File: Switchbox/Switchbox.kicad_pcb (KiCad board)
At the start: 4 copper layers, 90 x 68 mm, 42 parts, among them J1 USB-C_connector, SW1 SW_SPDT, SW2 SW_SPDT, SW3 SW_SPDT, SW4 SW_SPDT, SW5 SW_SPST_LED, SW6 SW_SPDT_BOX, U2 AP63203WU

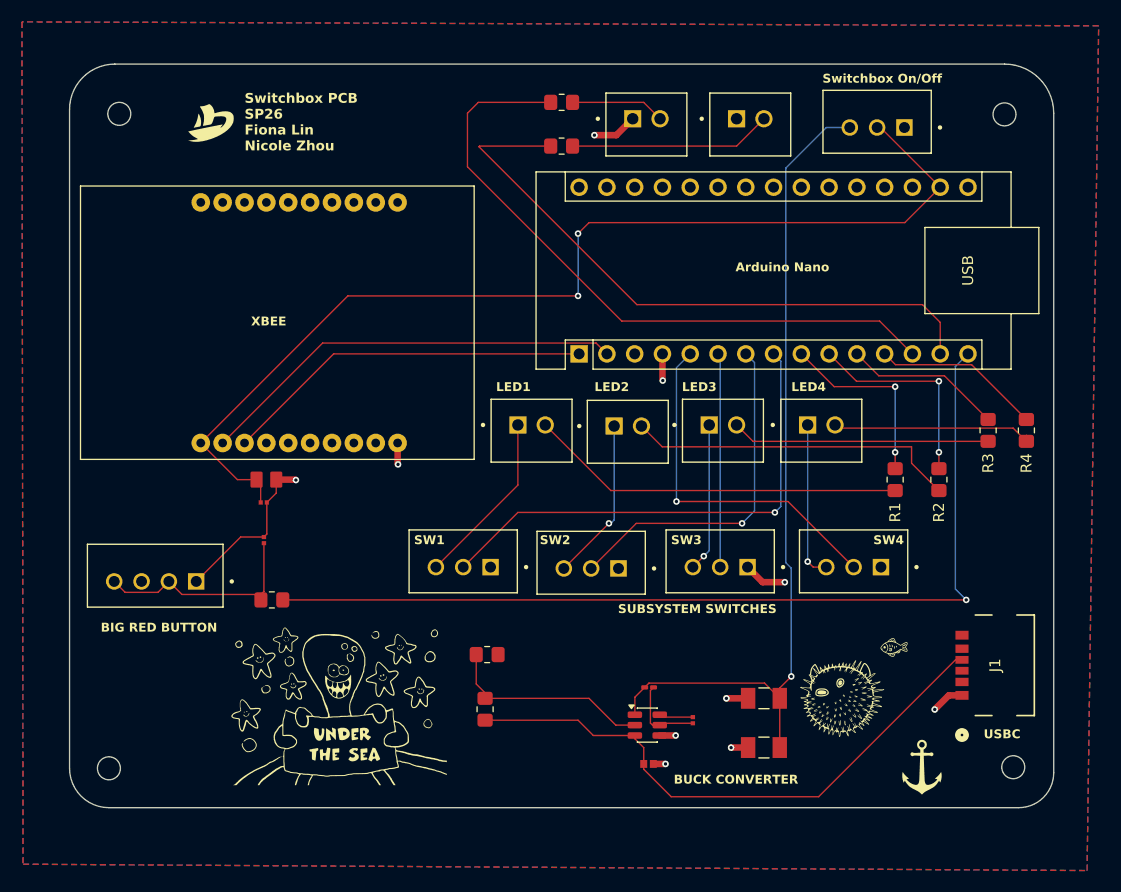
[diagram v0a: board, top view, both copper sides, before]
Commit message: Change USB signals, inductor footprint, add voltage divider between Xbee and Nano, route new components, increase trace widths
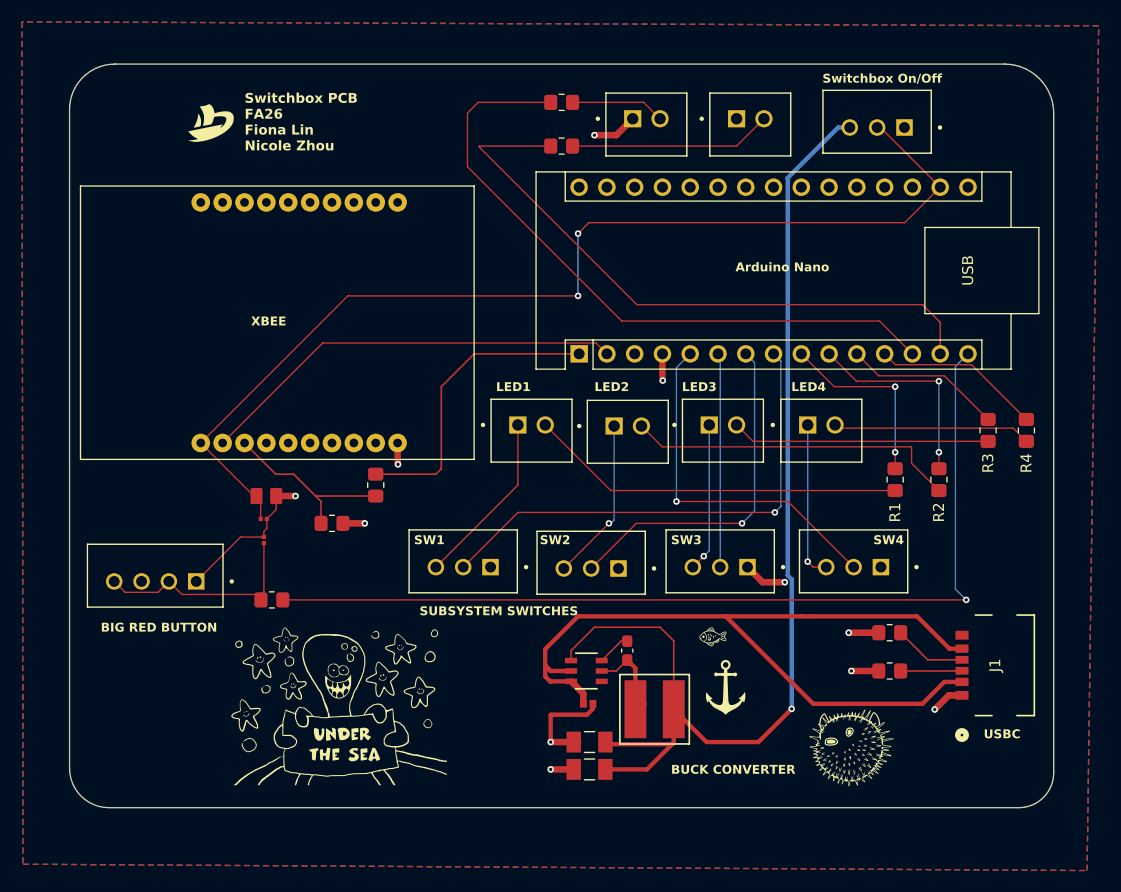
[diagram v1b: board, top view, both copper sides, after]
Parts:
- removed R3a1, R3b1: 100k, Resistor_SMD:R_0805_2012Metric_Pad1.20x1.40mm_HandSolder
- removed REF** (x4): MountingHole_2.1mm, MountingHole:MountingHole_2.1mm
- removed U2: AP63203WU, Package_TO_SOT_SMD:TSOT-23-6
- added R10: 20k, Resistor_SMD:R_0805_2012Metric_Pad1.20x1.40mm_HandSolder, F.Cu at (127.0, 127.0)
- added R11: 10k, Resistor_SMD:R_0805_2012Metric_Pad1.20x1.40mm_HandSolder, F.Cu at (131.0, 123.5)
- added R8: 5.1k, Resistor_SMD:R_0805_2012Metric_Pad1.20x1.40mm_HandSolder, F.Cu at (178.0, 140.5)
- added R9: 5.1k, Resistor_SMD:R_0805_2012Metric_Pad1.20x1.40mm_HandSolder, F.Cu at (178.0, 137.0)
- added U1: AP63203WU-7, switchbox_footprints:buck, F.Cu at (150.3, 140.5)
- C1: value 10µF -> 10 uF
- C2: value 0.1µF -> 100 nF; footprint switchbox_footprints:CAPC0603X33N -> Capacitor_SMD:C_0603_1608Metric_Pad1.08x0.95mm_HandSolder
- C3, C4: value 22µF -> 22 uF
- L1: value 4.7µH -> 3.9 uH; footprint Inductor_SMD:L_0201_0603Metric_Pad0.64x0.40mm_HandSolder -> switchbox_footprints:IND_BOURNS_SRR5018
- moved G*** 19.4 mm to (163.0, 142.0)
- moved C3 17.2 mm to (150.6, 149.5)
- moved G*** 16.6 mm to (162.0, 137.5)
- moved C4 16.0 mm to (150.6, 147.0)
- moved C2 8.75 mm to (154.0, 138.6)
- moved C1 7.79 mm to (150.4, 143.5)
- moved G*** 4.58 mm to (174.5, 147.5)
- moved L1 2.06 mm to (156.5, 144.0), turned to 0 degrees
- moved C5 1.50 mm to (120.8, 126.6)
- moved C6 1.50 mm to (121.0, 124.5)
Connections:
- J1 pad A12: unconnected-(J1-VBUS-PadA12) -> GND
- J1 pad A5: unconnected-(J1-CC1-PadA5) -> Net-(J1-CC1)
- J1 pad A9: unconnected-(J1-GND-PadA9) -> Sys_Vin
- J1 pad B5: Sys_Vin -> Net-(J1-CC2)
- J1 pad B9: unconnected-(J1-CC2-PadB9) -> Sys_Vin
- XBEE1 pad 3: TO_XBEE -> Net-(XBEE1-DIN/CONFIG)
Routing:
- net 3.3VBuck: track 77.0 -> 104.2 mm
- net Sys_Vin: track 53.0 -> 76.5 mm
- net Net-(U2-EN): track 19.0 -> 0.00 mm
- net Net-(XBEE1-DIN/CONFIG): track 0.00 -> 16.7 mm
- net GND: track 37.8 -> 49.1 mm, vias 10 -> 11
- net Net-(J1-CC2): track 0.00 -> 7.23 mm
- net TO_XBEE: track 34.0 -> 27.5 mm
- net Net-(J1-CC1): track 0.00 -> 6.35 mm
- net Net-(U1-SW): track 7.41 -> 8.52 mm
- net BOX_STATE: track 97.4 -> 98.0 mm
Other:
- board text added: "Switchbox PCB FA26 Fiona Lin Nicole Zhou"
- board text removed: "Switchbox PCB SP26 Fiona Lin Nicole Zhou"

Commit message: add usb-a
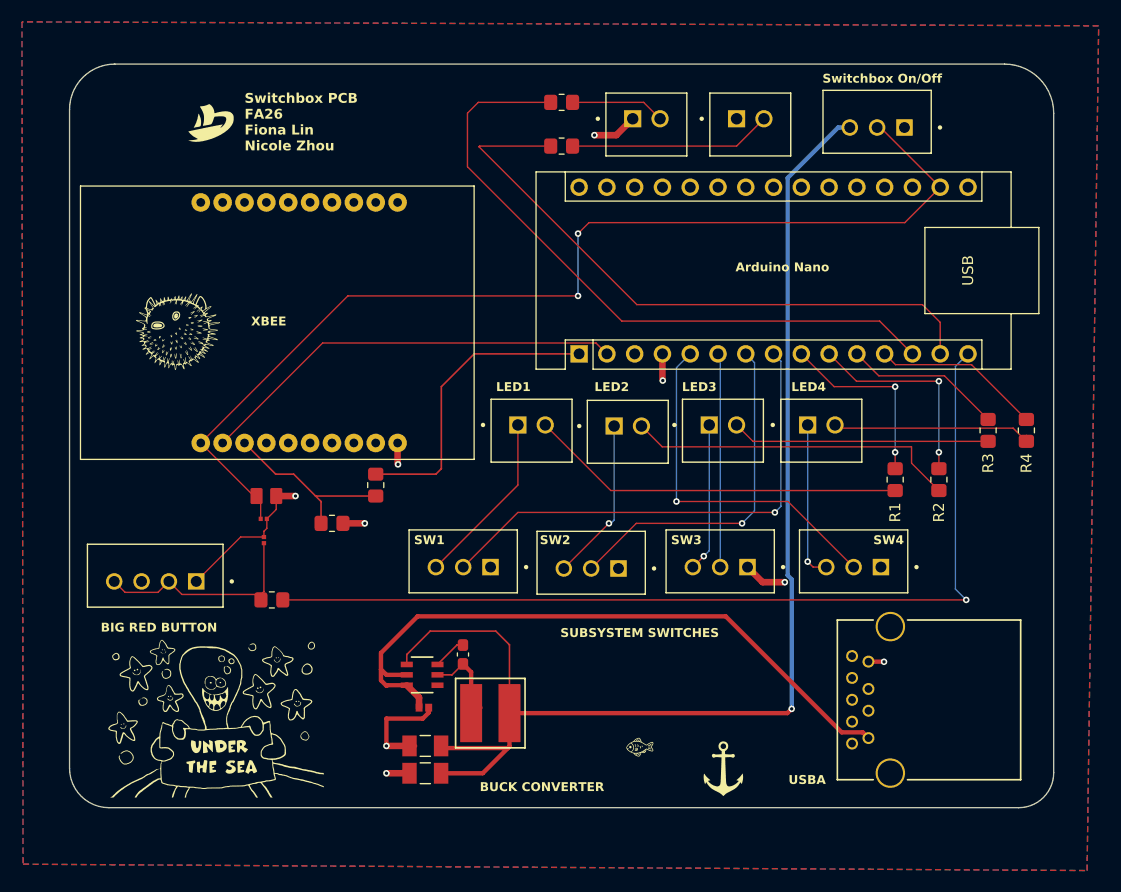
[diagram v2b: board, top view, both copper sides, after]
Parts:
- removed J1: USB-C_connector, switchbox_footprints:CONN_10164359-00011LF_AMP
- removed R8, R9: 5.1k, Resistor_SMD:R_0805_2012Metric_Pad1.20x1.40mm_HandSolder
- added J2: 484050003, switchbox_footprints:usba_footprint, F.Cu at (176.1, 146.6)
- moved G*** 72.4 mm to (112.9, 109.4)
- moved C2 15.0 mm to (139.0, 139.0)
- moved C3 15.0 mm to (135.5, 149.9)
- moved C4 15.0 mm to (135.5, 147.4)
- moved L1 15.0 mm to (141.5, 144.4)
- moved U1 15.0 mm to (135.2, 140.9)
- moved C1 15.0 mm to (135.4, 143.9)
- moved G*** 12.1 mm to (155.3, 147.6)
- moved G*** 11.3 mm to (116.2, 144.6)
- moved G*** 7.44 mm to (162.8, 149.4)
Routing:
- net Sys_Vin: track 76.5 -> 60.8 mm
- net 3.3VBuck: track 104.2 -> 116.9 mm
- net Net-(J1-CC2): track 7.23 -> 0.00 mm
- net GND: track 49.1 -> 42.3 mm, vias 11 -> 9
- net Net-(J1-CC1): track 6.35 -> 0.00 mm
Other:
- board text added: "USBA"
- board text removed: "USBC"

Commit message: Fix trace angles
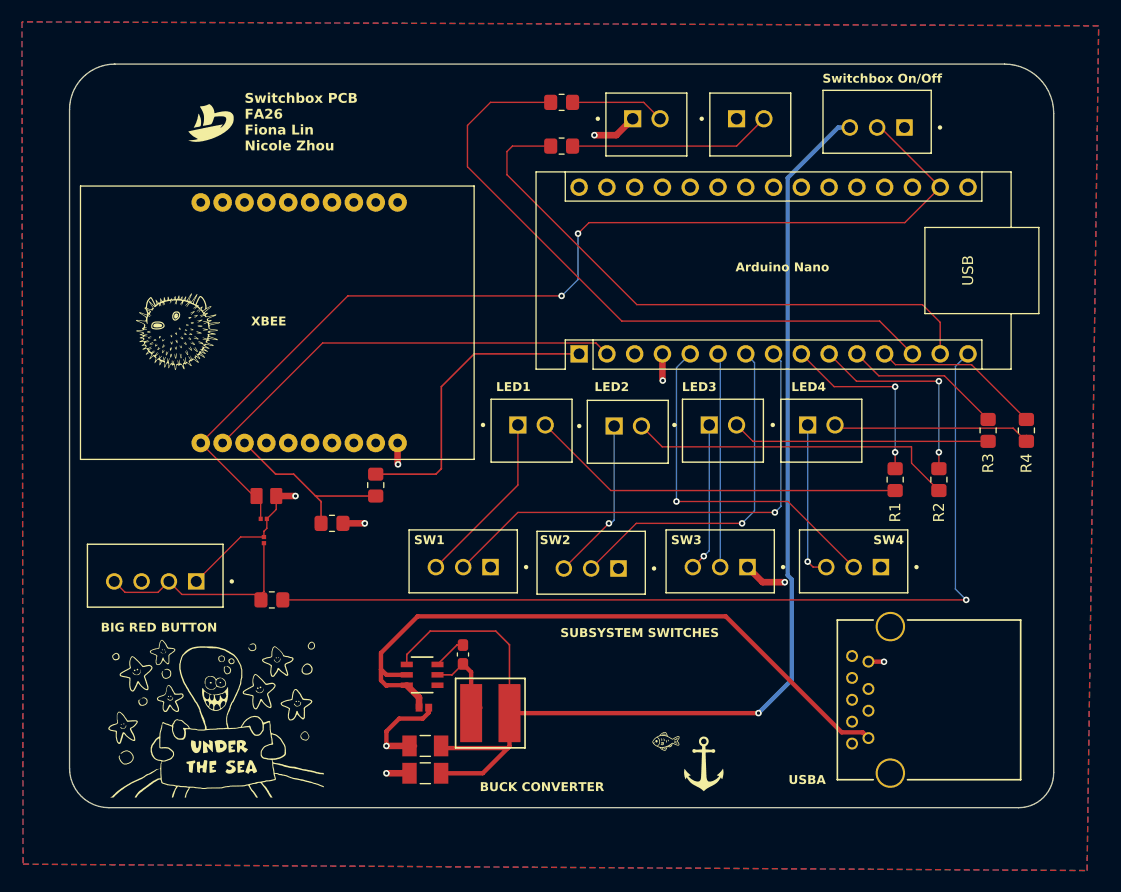
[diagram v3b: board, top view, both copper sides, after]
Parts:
- moved G*** 2.45 mm to (157.7, 147.1)
- moved G*** 1.84 mm to (161.0, 149.0)
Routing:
- net LED6_PWR: track 58.3 -> 54.4 mm
- net 3.3VBuck: track 116.9 -> 115.4 mm
- net BOX_STATE: track 98.0 -> 97.2 mm
- net GND: track 42.3 -> 41.6 mm
- net LED5_PWR: track 60.7 -> 60.0 mm
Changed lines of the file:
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@@
 	(footprint "LOGO"
 		(layer "F.Cu")
-		(at 155.32199 147.593737)
+		(at 157.71 147.06)
 		(property "Reference" "G***"
 			(at 0 0 0)
@@
 	(footprint "LOGO"
 		(layer "F.Cu")
-		(at 162.79 149.44)
+		(at 161 149)
 		(property "Reference" "G***"
 			(at 0 0 0)
@@
 	)
 	(segment
-		(start 181 107)
-		(end 182.62 108.62)
+		(start 143.5 92.5)
+		(end 143 93)
 		(width 0.127)
 		(layer "F.Cu")
@@
 	)
 	(segment
-		(start 140.5 92.5)
-		(end 147 92.5)
+		(start 143 93)
+		(end 143 95.12)
 		(width 0.127)
 		(layer "F.Cu")
@@
 	)
 	(segment
-		(start 140.44 92.56)
-		(end 154.88 107)
+		(start 182.62 108.62)
+		(end 182.62 111.5)
 		(width 0.127)
 		(layer "F.Cu")
@@
 	)
 	(segment
-		(start 154.88 107)
-		(end 181 107)
+		(start 181 107)
+		(end 182.62 108.62)
 		(width 0.127)
 		(layer "F.Cu")
@@
 	)
 	(segment
-		(start 182.62 108.62)
-		(end 182.62 111.5)
+		(start 143 95.12)
+		(end 154.88 107)
+		(width 0.127)
+		(layer "F.Cu")
+		(net 1)
+	)
+	(segment
+		(start 154.88 107)
+		(end 181 107)
 		(width 0.127)
 		(layer "F.Cu")
@@
 	)
 	(segment
-		(start 140.44 92.56)
-		(end 140.5 92.5)
+		(start 147 92.5)
+		(end 143.5 92.5)
 		(width 0.127)
 		(layer "F.Cu")
@@
 	)
 	(segment
-		(start 131.9774 144.85285)
-		(end 131.9774 147.35285)
+		(start 135.8399 144.31085)
+		(end 135.2979 144.85285)
 		(width 0.4)
 		(layer "F.Cu")
@@
 	)
 	(segment
-		(start 135.2979 144.85285)
-		(end 131.9774 144.85285)
-		(width 0.4)
-		(layer "F.Cu")
-		(net 6)
-	)
-	(segment
 		(start 130 127)
 		(end 128 127)
@@
 	)
 	(segment
+		(start 131.9774 146.0226)
+		(end 131.9774 147.35285)
+		(width 0.4)
+		(layer "F.Cu")
+		(net 6)
+	)
+	(segment
 		(start 176.059942 139.645001)
 		(end 177.465001 139.645001)
@@
 	)
 	(segment
-		(start 120.775 127.725)
-		(end 120.775 128.248)
-		(width 0.127)
+		(start 135.2979 144.85285)
+		(end 133.14715 144.85285)
+		(width 0.4)
 		(layer "F.Cu")
 		(net 6)
 	)
 	(segment
-		(start 135.8399 144.31085)
-		(end 135.2979 144.85285)
-		(width 0.4)
+		(start 120.775 127.725)
+		(end 120.775 128.248)
+		(width 0.127)
 		(layer "F.Cu")
 		(net 6)
@@
 	)
 	(segment
+		(start 135.8399 143.85285)
+		(end 135.8399 144.31085)
+		(width 0.4)
+		(layer "F.Cu")
+		(net 6)
+	)
+	(segment
 		(start 134.0854 147.35285)
 		(end 131.9774 147.35285)
@@
 	)
 	(segment
-		(start 135.8399 143.85285)
-		(end 135.8399 144.31085)
+		(start 133.14715 144.85285)
+		(end 131.9774 146.0226)
 		(width 0.4)
 		(layer "F.Cu")
@@
 	)
 	(segment
+		(start 148 106.2)
+		(end 128.45 106.2)
+		(width 0.127)
+		(layer "F.Cu")
+		(net 7)
+	)
+	(segment
 		(start 177.16 90.8)
 		(end 176.85 90.8)
@@
 	)
 	(segment
-		(start 149.5 106.2)
-		(end 128.45 106.2)
-		(width 0.127)
-		(layer "F.Cu")
-		(net 7)
-	)
-	(segment
 		(start 150.5 99.5)
 		(end 179.38 99.5)
@@
 	)
 	(via
-		(at 149.5 106.2)
+		(at 148 106.2)
 		(size 0.6)
 		(drill 0.3)
@@
 	(segment
 		(start 149.5 100.5)
-		(end 149.5 106.2)
+		(end 149.5 104.7)
+		(width 0.127)
+		(layer "B.Cu")
+		(net 7)
+	)
+	(segment
+		(start 149.5 104.7)
+		(end 148 106.2)
 		(width 0.127)
 		(layer "B.Cu")
@@
 	)
 	(segment
-		(start 140.38 88.5)
-		(end 139.3885 89.4915)
+		(start 141.5 88.5)
+		(end 139.3885 90.6115)
 		(width 0.127)
 		(layer "F.Cu")
@@
 	)
 	(segment
-		(start 139.3885 94.3885)
-		(end 153.5 108.5)
+		(start 139.3885 90.6115)
+		(end 139.3885 94.3885)
 		(width 0.127)
 		(layer "F.Cu")
@@
 	)
 	(segment
-		(start 140.38 88.5)
-		(end 147 88.5)
+		(start 139.3885 94.3885)
+		(end 153.5 108.5)
 		(width 0.127)
 		(layer "F.Cu")
@@
 	)
 	(segment
-		(start 139.3885 89.4915)
-		(end 139.3885 94.3885)
+		(start 147 88.5)
+		(end 141.5 88.5)
 		(width 0.127)
 		(layer "F.Cu")
@@
 	)
 	(segment
+		(start 166 144.35285)
+		(end 143.23 144.35285)
+		(width 0.4)
+		(layer "F.Cu")
+		(net 43)
+	)
+	(segment
 		(start 133.8399 138.99035)
 		(end 135.9774 136.85285)
@@
 	)
 	(segment
-		(start 168.64715 144.35285)
-		(end 143.23 144.35285)
-		(width 0.4)
-		(layer "F.Cu")
-		(net 43)
-	)
-	(segment
-		(start 169.038 143.962)
-		(end 168.64715 144.35285)
-		(width 0.4)
-		(layer "F.Cu")
-		(net 43)
-	)
-	(segment
 		(start 140.7843 149.85285)
 		(end 143.23 147.40715)
@@
 	)
 	(via
-		(at 169.038 143.962)
+		(at 166 144.35285)
 		(size 0.6)
 		(drill 0.3)
@@
 	(segment
 		(start 168.670127 131.752)
-		(end 169.038 132.119873)
+		(end 168.670127 95.413556)
 		(width 0.4)
 		(layer "B.Cu")
@@
 	)
 	(segment
-		(start 174.35 90.8)
-		(end 173.283683 90.8)
+		(start 166 144.35285)
+		(end 169.038 141.31485)
 		(width 0.4)
 		(layer "B.Cu")
@@
 	)
 	(segment
-		(start 168.670127 95.413556)
-		(end 168.670127 131.752)
+		(start 169.038 141.31485)
+		(end 169.038 132.119873)
 		(width 0.4)
 		(layer "B.Cu")
@@
 	(segment
 		(start 173.283683 90.8)
-		(end 168.670127 95.413556)
+		(end 174.35 90.8)
+		(width 0.4)
+		(layer "B.Cu")
+		(net 43)
+	)
+	(segment
+		(start 168.670127 95.413556)
+		(end 173.283683 90.8)
 		(width 0.4)
 		(layer "B.Cu")
@@
 	(segment
 		(start 169.038 132.119873)
-		(end 169.038 143.962)
+		(end 168.670127 131.752)
 		(width 0.4)
 		(layer "B.Cu")
@@
 		(min_thickness 0.25)
 		(filled_areas_thickness no)
-		(fill yes
+		(fill
 			(thermal_gap 0.5)
 			(thermal_bridge_width 0.5)

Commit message: new buck
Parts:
- moved C2 8.25 mm to (131.0, 141.2)
- moved C4 5.05 mm to (140.4, 145.9)
- moved C1 4.97 mm to (136.9, 139.1), turned to 180 degrees
- moved C3 4.01 mm to (135.1, 145.9), turned to 0 degrees
- moved L1 3.44 mm to (141.9, 140.9)
- moved U1 1.25 mm to (135.3, 142.1)
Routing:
- net 3.3VBuck: track 115.4 -> 104.7 mm, vias 1 -> 3
- net Sys_Vin: track 60.8 -> 51.8 mm, vias 0 -> 2
- net GND: track 41.6 -> 44.8 mm, vias 9 -> 13
- net Net-(U1-BST): track 3.07 -> 6.08 mm
- net BUTTON: track 85.9 -> 83.3 mm
- net Net-(U1-SW): track 8.52 -> 10.9 mm
- net LED1_PWR: track 17.4 -> 16.2 mm
- net LED2_PWR: track 19.1 -> 18.0 mm
- net LED4_STATE: track 32.7 -> 31.7 mm
- net LED6_PWR: track 54.4 -> 53.8 mm
- net (no net): vias 0 -> 4
